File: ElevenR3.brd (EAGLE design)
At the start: 68.6 x 53.3 mm, 63 parts, among them IC1 ATMEGA328P, IC2 ATMEGA8U2-MU, IC3 MC33269DT-5.0, IC4 LM358D, IC5 LP2985-33DBVR, J2 Analog, J3 Digital_8_13, J4 Digital_0_7, J5 DC_2_1MM, J6 Digital_0_7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

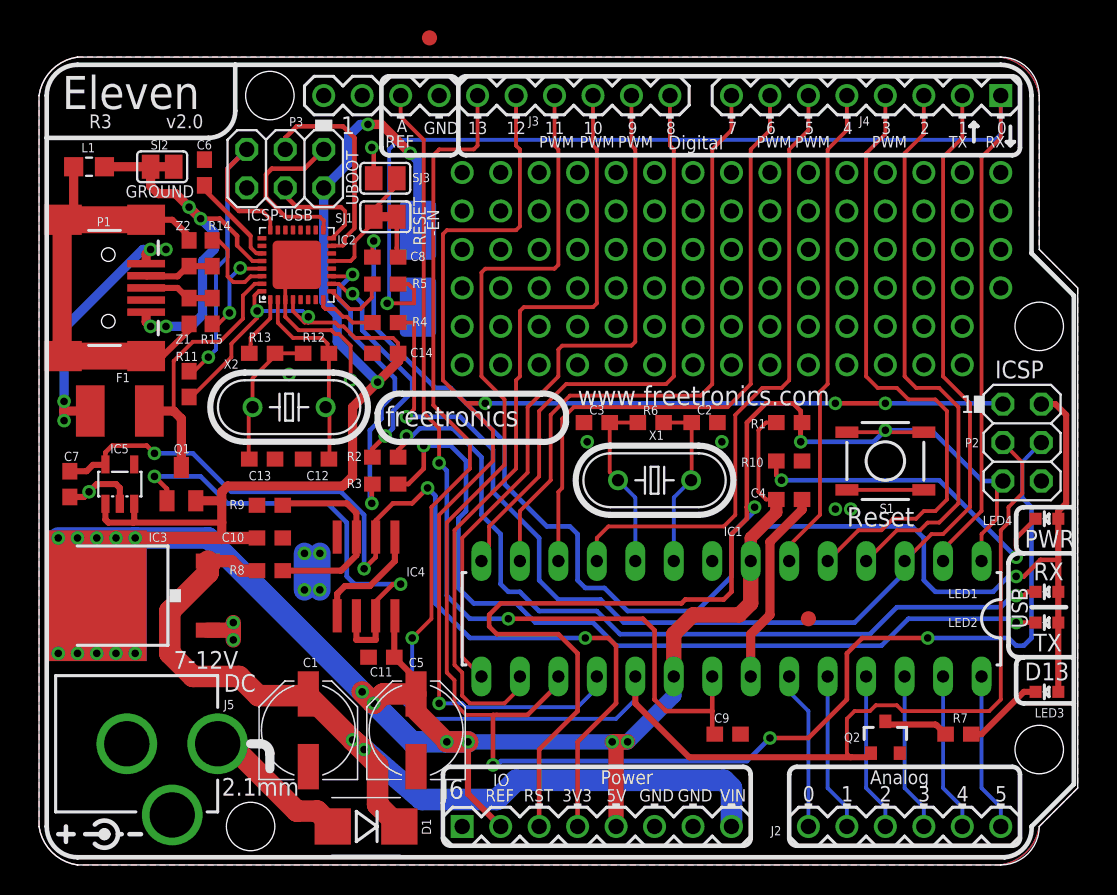
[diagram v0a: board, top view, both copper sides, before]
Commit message: Routed I2C and converted to microUSB
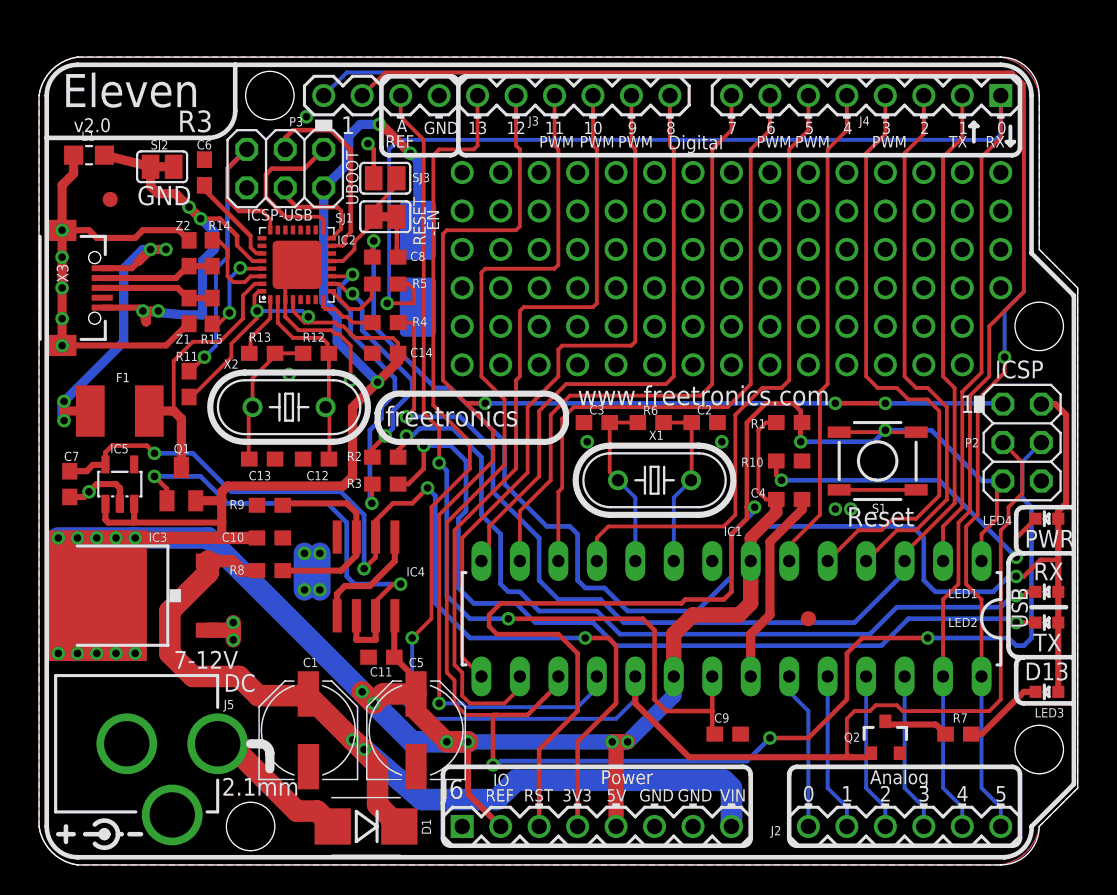
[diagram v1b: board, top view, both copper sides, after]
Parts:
- removed P1: USB-FT, freetronics-master-v1:USB-MINIB-FT
- added X3: USBSF-MICROB, freetronics-jon:USB-MICROB
- moved U$5 23.6 mm to (4.70, 43.9)
- moved L1 0.76 mm to (3.30, 46.9)
- moved S1 0.51 mm to (55.4, 26.7)
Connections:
- net GND: now also X3.GND; no longer P1.GND
- net N$115: now also X3.VBUS; no longer P1.VBUS
- net N$16: now also X3.D+; no longer P1.D+
- net N$17: now also X3.D-; no longer P1.D-
- net N$3: now also X3.MT1, X3.MT2; no longer P1.SH1, P1.SH2, P1.SH3, P1.SH4
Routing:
- net A5_SCL: track 10.4 -> 98.7 mm, vias 0 -> 1
- net A4_SDA: track 10.4 -> 96.4 mm
- net GND: track 73.8 -> 77.5 mm, vias 18 -> 19
- net N$17: track 4.65 -> 7.58 mm
- net N$16: track 4.64 -> 7.54 mm
- net N$115: track 20.3 -> 23.1 mm
- net D2: track 37.5 -> 35.8 mm
- net D1_TX: track 85.6 -> 84.3 mm
- net D3: track 40.7 -> 39.6 mm
- net SCK2: track 14.1 -> 13.1 mm
- net N$3: track 31.0 -> 31.1 mm, vias 0 -> 5
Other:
- board text removed: "GROUND"

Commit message: Overlay, layout, and schematic tweaks
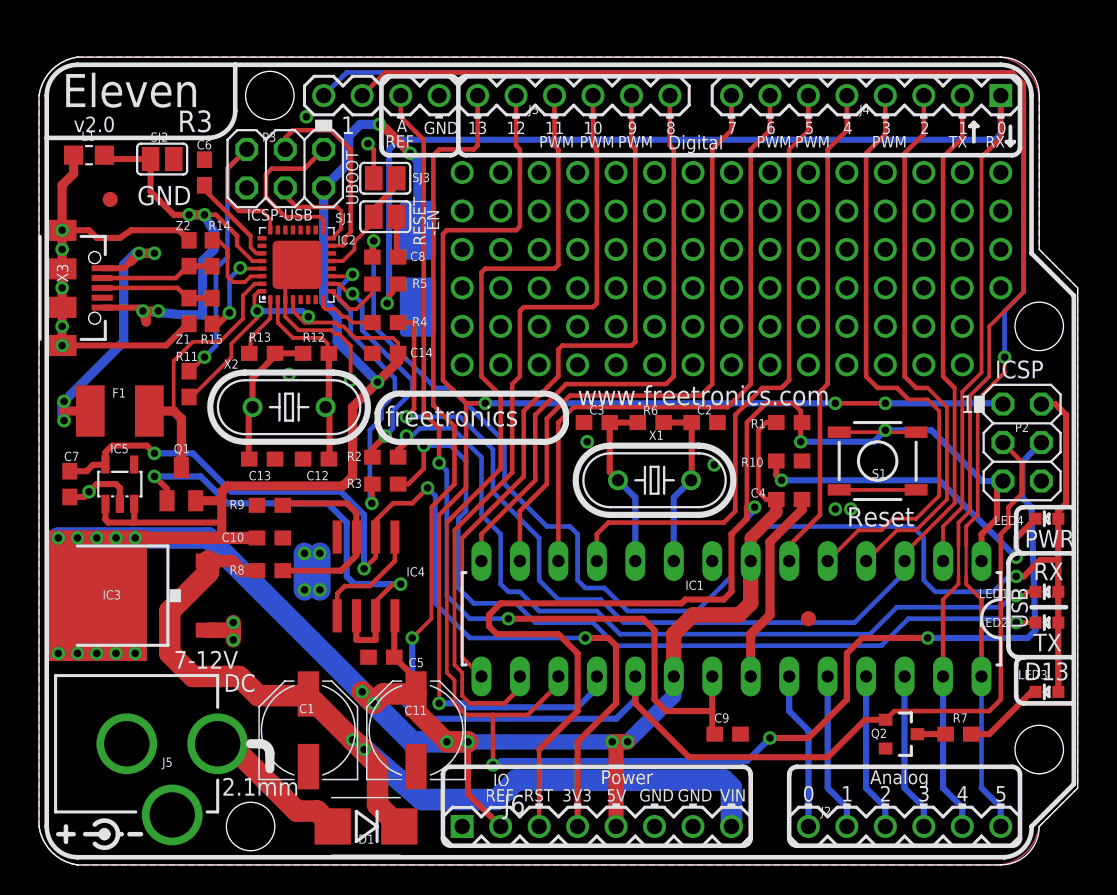
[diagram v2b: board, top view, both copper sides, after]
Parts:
- IC2: value ATMEGA8U2-MU -> ATMEGA16U2-MU
- moved Q2 1.05 mm to (56.9, 8.64), turned to 270 degrees
- moved SJ2 0.51 mm to (8.13, 46.6)
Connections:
- new net N$1: C8.1, SJ1.2
- new net N$116: IC2.28, L1.2, SJ2.1, X3.GND
- net DTR: no longer C8.1, SJ1.2
- net GND: no longer IC2.28, L1.2, SJ2.1, X3.GND
- net N$3: now also X3.FIX1, X3.FIX2, X3.TAB1, X3.TAB2; no longer X3.MT1, X3.MT2
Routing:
- net GND: track 77.5 -> 44.7 mm, vias 19 -> 15
- net N$116: track 0.00 -> 32.1 mm, vias 0 -> 4
- net D13_SCK: track 113.8 -> 109.4 mm
- net DTR: track 11.9 -> 7.68 mm
- net N$1: track 0.00 -> 2.70 mm
- net N$6: track 4.32 -> 1.86 mm
- net D0_RX: track 89.7 -> 87.4 mm
- net N$115: track 23.1 -> 21.3 mm
- net D12_MISO: track 95.1 -> 93.7 mm
- net D11_MOSI: track 114.2 -> 113.5 mm

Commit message: Routing, position, and overlay tweaks
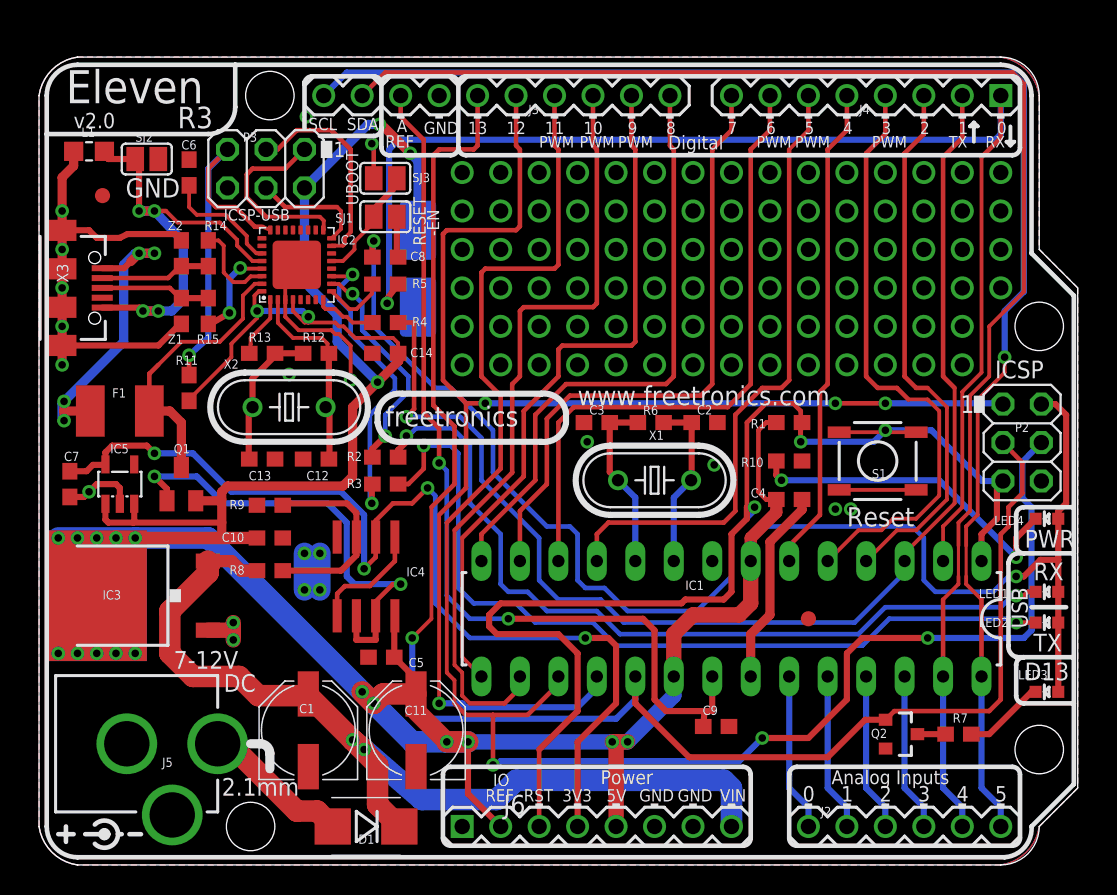
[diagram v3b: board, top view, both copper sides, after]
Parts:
- moved P3 1.27 mm to (15.0, 46.0)
- moved C6 1.02 mm to (9.91, 45.7)
- moved SJ2 1.02 mm to (7.11, 46.6)
- moved C9 0.92 mm to (44.7, 9.14)
- moved U$5 0.57 mm to (4.19, 44.2)
- moved Z1 0.51 mm to (9.40, 36.6)
- moved Z2 0.51 mm to (9.40, 40.4)
- moved R11 0.25 mm to (9.91, 31.5)
- moved R14 0.25 mm to (11.2, 40.4)
- moved R15 0.25 mm to (11.2, 36.6)
- moved L1 0.25 mm to (3.30, 47.1)
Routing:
- net N$117: track 6.30 -> 7.81 mm
- net MISO2: track 11.1 -> 12.4 mm
- net N$116: track 32.1 -> 30.8 mm
- net MOSI2: track 6.68 -> 7.65 mm
- net USBVCC: track 17.7 -> 18.6 mm
- net 5V: track 246.7 -> 247.6 mm
- net SCK2: track 13.1 -> 14.0 mm
- net AREF: track 61.6 -> 60.9 mm
- net D13_SCK: track 109.4 -> 108.8 mm
- net RESET2: track 24.2 -> 24.7 mm
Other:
- board text added: "Analog Inputs"
- board text added: "SCL"
- board text added: "SDA"
- board text removed: "Analog"
- board text removed: "v1.0"

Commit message: Clearances
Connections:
- net N$116 renamed UGND
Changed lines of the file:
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@@
 <wire x1="7.62" y1="27.178" x2="10.16" y2="27.178" width="0.4064" layer="16"/>
 <wire x1="10.16" y1="27.178" x2="12.7" y2="24.638" width="0.4064" layer="16"/>
-<wire x1="12.7" y1="24.638" x2="19.939" y2="24.638" width="0.4064" layer="16"/>
-<wire x1="19.939" y1="24.638" x2="21.463" y2="23.114" width="0.4064" layer="16"/>
-<wire x1="21.463" y1="23.114" x2="21.463" y2="19.558" width="0.4064" layer="16"/>
+<wire x1="12.7" y1="24.638" x2="19.685" y2="24.638" width="0.4064" layer="16"/>
+<wire x1="19.685" y1="24.638" x2="21.463" y2="22.86" width="0.4064" layer="16"/>
+<wire x1="21.463" y1="22.86" x2="21.463" y2="19.558" width="0.4064" layer="16"/>
 <wire x1="21.463" y1="19.558" x2="22.225" y2="20.32" width="0.3048" layer="1"/>
 <wire x1="22.225" y1="20.32" x2="22.225" y2="21.65" width="0.3048" layer="1"/>
@@
 <contactref element="C1" pad="+"/>
 <contactref element="R8" pad="2"/>
-<wire x1="14.478" y1="11.176" x2="17.694" y2="11.176" width="1.4224" layer="1"/>
-<wire x1="13.208" y1="12.446" x2="14.478" y2="11.176" width="1.4224" layer="1"/>
-<wire x1="10.16" y1="12.446" x2="13.208" y2="12.446" width="1.4224" layer="1"/>
+<wire x1="16.002" y1="11.176" x2="17.694" y2="11.176" width="1.4224" layer="1"/>
+<wire x1="14.732" y1="12.446" x2="16.002" y2="11.176" width="1.4224" layer="1"/>
+<wire x1="10.16" y1="12.446" x2="14.732" y2="12.446" width="1.4224" layer="1"/>
 <wire x1="8.636" y1="13.97" x2="10.16" y2="12.446" width="1.4224" layer="1"/>
 <wire x1="8.636" y1="13.97" x2="8.636" y2="16.764" width="1.4224" layer="1"/>
@@
 <wire x1="22.987" y1="37.084" x2="23.114" y2="37.338" width="0.254" layer="16"/>
 <wire x1="23.114" y1="37.338" x2="23.114" y2="47.244" width="0.4064" layer="16"/>
-<wire x1="23.114" y1="47.244" x2="23.749" y2="47.879" width="0.4064" layer="16"/>
-<wire x1="23.749" y1="47.879" x2="63.119" y2="47.879" width="0.4064" layer="16"/>
-<wire x1="63.119" y1="47.879" x2="63.5" y2="48.26" width="0.4064" layer="16"/>
-<wire x1="63.5" y1="48.26" x2="63.5" y2="50.8" width="0.4064" layer="16"/>
+<wire x1="23.114" y1="47.244" x2="24.003" y2="48.133" width="0.4064" layer="16"/>
+<wire x1="24.003" y1="48.133" x2="63.119" y2="48.133" width="0.4064" layer="16"/>
+<wire x1="63.119" y1="48.133" x2="63.5" y2="48.514" width="0.4064" layer="16"/>
+<wire x1="63.5" y1="48.514" x2="63.5" y2="50.8" width="0.4064" layer="16"/>
 <via x="22.987" y="37.084" extent="1-16" drill="0.5"/>
 <wire x1="22.987" y1="37.084" x2="22.987" y2="37.377" width="0.4064" layer="1"/>
@@
 <wire x1="27.432" y1="28.956" x2="26.035" y2="30.353" width="0.3048" layer="1"/>
 <wire x1="27.432" y1="25.146" x2="27.432" y2="28.956" width="0.3048" layer="1"/>
-<wire x1="25.908" y1="23.622" x2="27.432" y2="25.146" width="0.3048" layer="1"/>
-<wire x1="25.908" y1="16.256" x2="25.908" y2="23.622" width="0.254" layer="1"/>
-<wire x1="24.638" y1="14.986" x2="25.908" y2="16.256" width="0.254" layer="1"/>
+<wire x1="25.146" y1="15.494" x2="25.146" y2="22.86" width="0.3048" layer="1"/>
+<wire x1="24.638" y1="14.986" x2="25.146" y2="15.494" width="0.3048" layer="1"/>
 <wire x1="24.638" y1="10.414" x2="24.638" y2="14.986" width="0.4064" layer="16"/>
 <wire x1="25.4" y1="9.652" x2="24.638" y2="10.414" width="0.4064" layer="16"/>
@@
 <wire x1="52.07" y1="7.112" x2="54.544" y2="9.586" width="0.4064" layer="1"/>
 <wire x1="54.544" y1="9.586" x2="55.896" y2="9.586" width="0.4064" layer="1"/>
+<wire x1="25.146" y1="22.86" x2="26.162" y2="23.876" width="0.3048" layer="1"/>
+<wire x1="27.432" y1="25.146" x2="26.162" y2="23.876" width="0.3048" layer="1"/>
 </signal>
 <signal name="D12_MISO">
@@
 <wire x1="28.194" y1="30.48" x2="26.67" y2="32.004" width="0.3048" layer="1"/>
 <wire x1="28.194" y1="24.892" x2="28.194" y2="30.48" width="0.3048" layer="1"/>
-<wire x1="26.416" y1="23.114" x2="28.194" y2="24.892" width="0.3048" layer="1"/>
 <wire x1="26.416" y1="10.668" x2="26.416" y2="23.114" width="0.254" layer="1"/>
 <wire x1="26.416" y1="10.668" x2="27.94" y2="10.668" width="0.4064" layer="16"/>
@@
 <via x="29.464" y="30.48" extent="1-16" drill="0.5"/>
 <wire x1="28.194" y1="30.48" x2="29.464" y2="30.48" width="0.3048" layer="1"/>
+<wire x1="26.416" y1="23.114" x2="26.67" y2="23.368" width="0.254" layer="1"/>
+<wire x1="28.194" y1="24.892" x2="26.67" y2="23.368" width="0.3048" layer="1"/>
 </signal>
 <signal name="D11_MOSI">
@@
 <wire x1="30.48" y1="30.988" x2="29.21" y2="32.258" width="0.3048" layer="1"/>
 <wire x1="30.48" y1="26.162" x2="30.48" y2="30.988" width="0.3048" layer="1"/>
-<wire x1="26.924" y1="22.606" x2="30.48" y2="26.162" width="0.3048" layer="1"/>
 <wire x1="26.924" y1="12.7" x2="26.924" y2="22.606" width="0.254" layer="1"/>
 <wire x1="28.194" y1="9.906" x2="27.432" y2="10.668" width="0.3048" layer="1"/>
@@
 <via x="47.752" y="8.382" extent="1-16" drill="0.5"/>
 <via x="29.972" y="6.604" extent="1-16" drill="0.5"/>
+<wire x1="26.924" y1="22.606" x2="27.178" y2="22.86" width="0.254" layer="1"/>
+<wire x1="30.48" y1="26.162" x2="27.178" y2="22.86" width="0.3048" layer="1"/>
 </signal>
 <signal name="D10">
@@
 <wire x1="31.242" y1="31.75" x2="31.75" y2="32.258" width="0.3048" layer="1"/>
 <wire x1="31.242" y1="25.908" x2="31.242" y2="31.75" width="0.3048" layer="1"/>
-<wire x1="27.432" y1="22.098" x2="31.242" y2="25.908" width="0.3048" layer="1"/>
 <wire x1="27.432" y1="13.208" x2="27.432" y2="22.098" width="0.254" layer="1"/>
 <wire x1="27.432" y1="13.208" x2="27.94" y2="12.7" width="0.254" layer="1"/>
@@
 <wire x1="30.734" y1="10.668" x2="31.75" y2="11.684" width="0.3048" layer="1"/>
 <wire x1="31.75" y1="11.684" x2="31.75" y2="12.446" width="0.254" layer="1"/>
+<wire x1="27.432" y1="22.098" x2="27.686" y2="22.352" width="0.254" layer="1"/>
+<wire x1="31.242" y1="25.908" x2="27.686" y2="22.352" width="0.3048" layer="1"/>
 </signal>
 <signal name="D9">
@@
 <wire x1="32.004" y1="29.972" x2="34.29" y2="32.258" width="0.3048" layer="1"/>
 <wire x1="32.004" y1="25.654" x2="32.004" y2="29.972" width="0.3048" layer="1"/>
-<wire x1="27.94" y1="21.59" x2="32.004" y2="25.654" width="0.3048" layer="1"/>
 <wire x1="27.94" y1="13.716" x2="27.94" y2="21.59" width="0.254" layer="1"/>
 <wire x1="29.21" y1="12.446" x2="27.94" y2="13.716" width="0.254" layer="1"/>
+<wire x1="27.94" y1="21.59" x2="28.194" y2="21.844" width="0.254" layer="1"/>
+<wire x1="32.004" y1="25.654" x2="28.194" y2="21.844" width="0.3048" layer="1"/>
 </signal>
 <signal name="D8">
@@
 <wire x1="12.446" y1="47.244" x2="11.176" y2="45.974" width="0.3048" layer="1"/>
 <wire x1="11.176" y1="45.974" x2="11.176" y2="43.942" width="0.3048" layer="1"/>
-<wire x1="11.176" y1="43.942" x2="11.684" y2="43.434" width="0.3048" layer="1"/>
-<wire x1="11.684" y1="43.434" x2="12.954" y2="43.434" width="0.3048" layer="1"/>
+<wire x1="11.176" y1="43.942" x2="11.684" y2="43.434" width="0.254" layer="1"/>
+<wire x1="11.684" y1="43.434" x2="12.954" y2="43.434" width="0.254" layer="1"/>
 <wire x1="14.76" y1="42.136" x2="15.268" y2="41.924" width="0.254" layer="1"/>
 <wire x1="9.906" y1="33.655" x2="11.176" y2="34.798" width="0.4064" layer="16"/>
@@
 <via x="9.906" y="33.655" extent="1-16" drill="0.5"/>
 <wire x1="9.906" y1="33.655" x2="9.906" y2="32.346" width="0.3048" layer="1"/>
-<wire x1="12.954" y1="43.434" x2="14.252" y2="42.136" width="0.3048" layer="1"/>
-<wire x1="14.252" y1="42.136" x2="14.76" y2="42.136" width="0.3048" layer="1"/>
+<wire x1="12.954" y1="43.434" x2="14.252" y2="42.136" width="0.254" layer="1"/>
+<wire x1="14.252" y1="42.136" x2="14.76" y2="42.136" width="0.254" layer="1"/>
 </signal>
 <signal name="N$113">
@@
 <wire x1="23.622" y1="40.22" x2="23.622" y2="42.799" width="0.4064" layer="1"/>
 </signal>
-<signal name="N$116">
+<signal name="UGND">
 <contactref element="L1" pad="2"/>
 <contactref element="IC2" pad="28"/>
@@
 </signal>
 </signals>
+<errors>
+</errors>
 </board>
 </drawing>
